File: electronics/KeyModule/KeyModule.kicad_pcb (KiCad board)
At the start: 2 copper layers, 20 x 100 mm, 23 parts, among them SW1 SW_Push, SW2 SW_Push, SW3 SW_Push, SW4 SW_Push, SW5 SW_Push, U1 74HC165

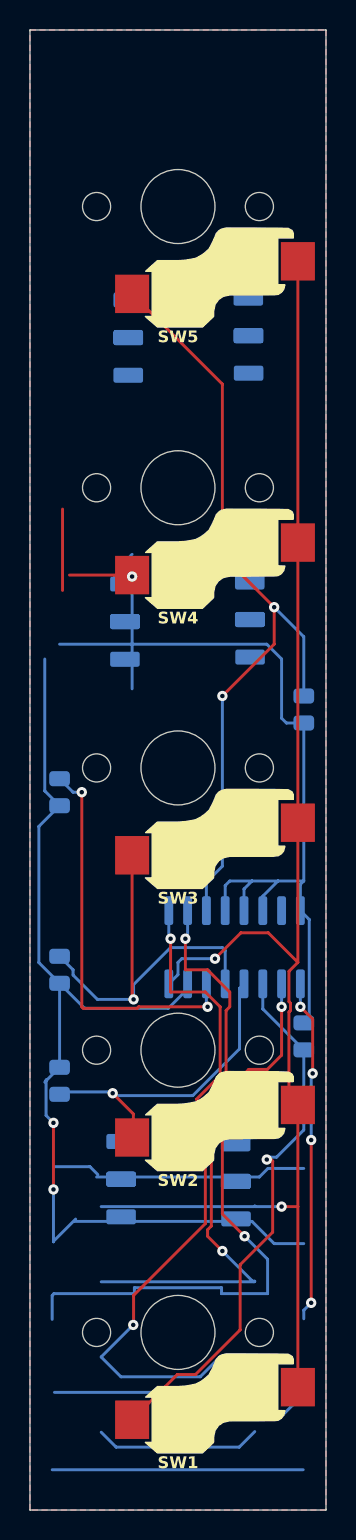
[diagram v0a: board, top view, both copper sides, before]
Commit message: Place the Harwin connectors and narrow the key module to 16.5 mm
Board edges move in to 70.55 and 87.05 (keys unchanged), the twelve
2-pin placeholders are gone, and J_LEFT1..3 / J_RIGHT1..3 sit on the
back in the gaps between keys at the offsets from Electronics.md.
Pull-downs R2..R5 move to a column at x=73 beside U1. The header
footprint now numbers its pads from +x so pin 1 is topmost on both
edges once the board is flipped. Routing is untouched and now stale.

Co-Authored-By: Claude Fable 5.1 <noreply@anthropic.com>
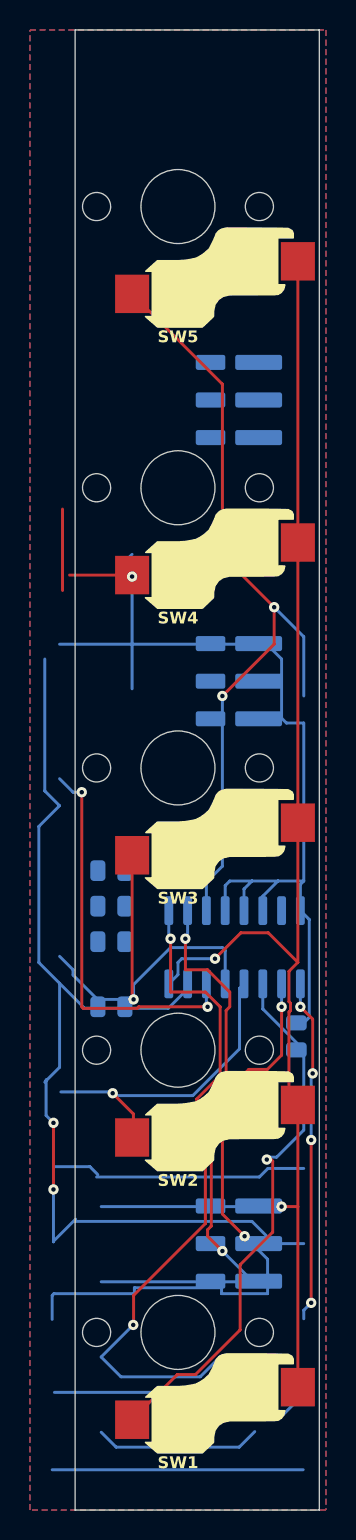
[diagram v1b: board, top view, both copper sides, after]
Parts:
- removed REF** (x12): CONN_SMD2, Library:CONN_SMD2
- added J_LEFT1: M20-7910342R, Library:Harwin_M20-791_1x03_Horizontal_SMD, B.Cu at (79.7, 65.0)
- added J_LEFT2: M20-7910342R, Library:Harwin_M20-791_1x03_Horizontal_SMD, B.Cu at (79.7, 84.0)
- added J_LEFT3: M20-7910342R, Library:Harwin_M20-791_1x03_Horizontal_SMD, B.Cu at (79.7, 122.0)
- added J_RIGHT1: M20-8890345R, Library:Harwin_M20-889_1x03_Horizontal_SMD, B.Cu at (83.0, 65.0)
- added J_RIGHT2: M20-8890345R, Library:Harwin_M20-889_1x03_Horizontal_SMD, B.Cu at (83.0, 84.0)
- added J_RIGHT3: M20-8890345R, Library:Harwin_M20-889_1x03_Horizontal_SMD, B.Cu at (83.0, 122.0)
- moved R5 17.0 mm to (73.0, 96.8), turned to 0 degrees
- moved R4 8.46 mm to (73.0, 99.2), turned to 0 degrees
- moved R2 6.10 mm to (73.0, 106.0), turned to 0 degrees
- moved R3 3.98 mm to (73.0, 101.6), turned to 0 degrees
- moved R1 0.50 mm to (85.5, 108.0)
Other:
- board size 20 x 100 mm -> 16.5 x 100 mm
